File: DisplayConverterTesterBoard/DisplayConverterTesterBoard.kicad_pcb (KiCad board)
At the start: 2 copper layers, 37 x 36 mm, 25 parts, among them J2 Conn_01x07, J3 Conn_01x03, J4 FPC 20PIN P0.5mm, J5 BM20B(0.8)-10DS-0.4V, J6 Conn_01x03, J7 FPC 10PIN P0.5mm, U2 TPS61040DBV

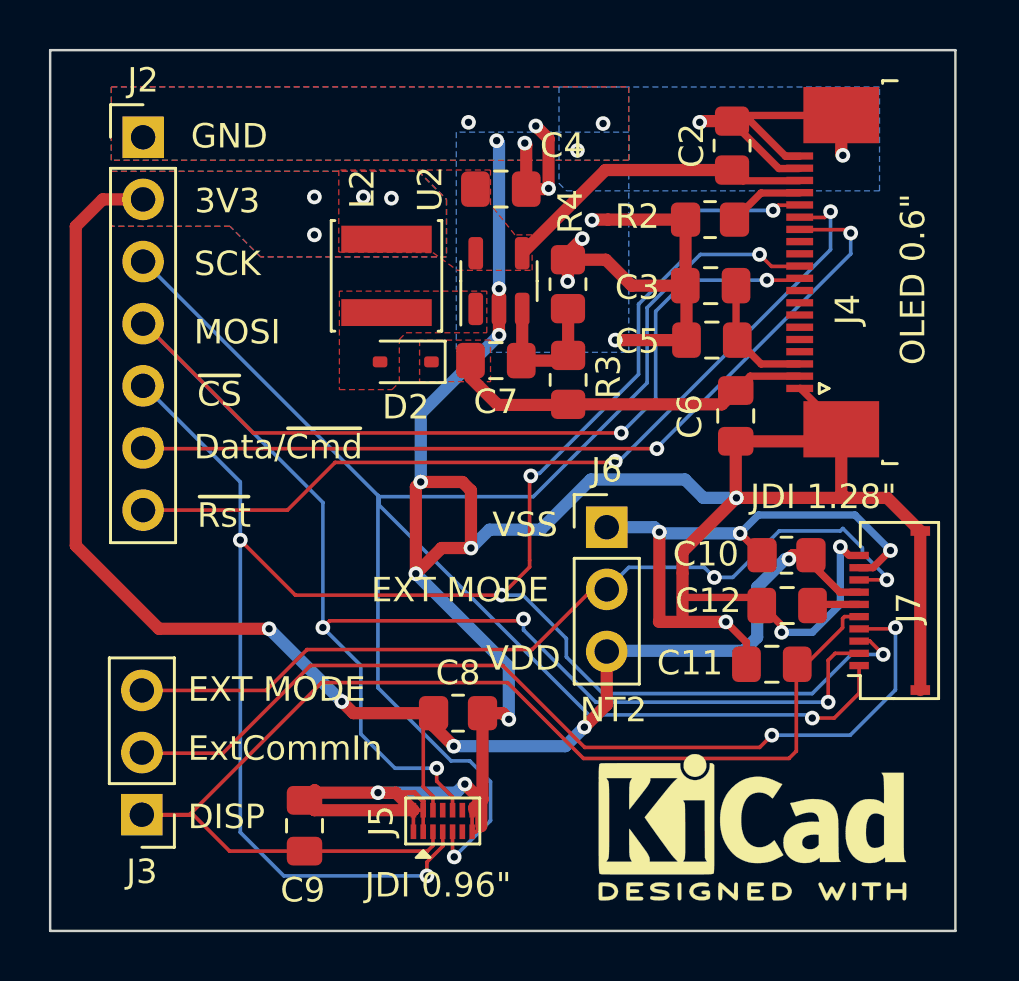
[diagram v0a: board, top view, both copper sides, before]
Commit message: updated Diode footprint. fix GND routing
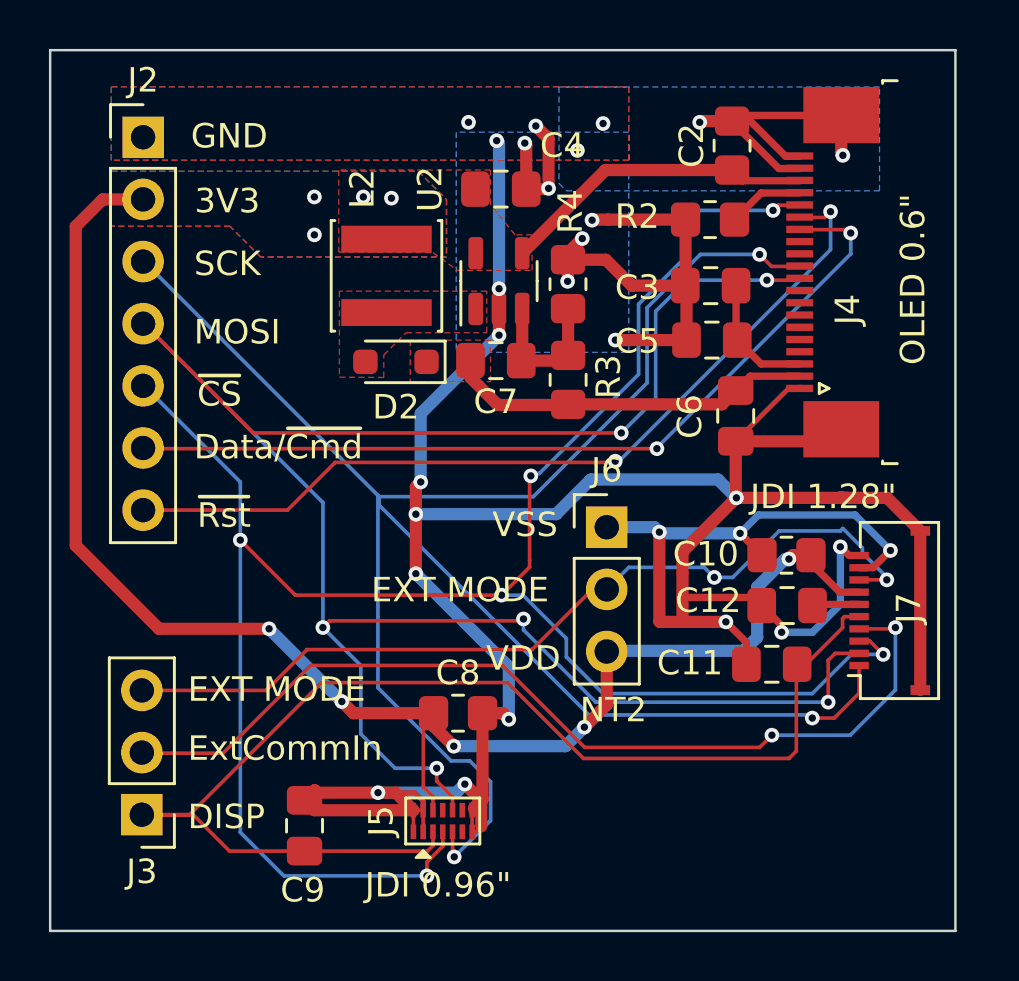
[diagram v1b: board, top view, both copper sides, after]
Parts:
- removed REF**: KiCad-Logo2_5mm_SilkScreen, Symbol:KiCad-Logo2_5mm_SilkScreen
- D2: footprint Diode_SMD:D_SOD-323 -> Diode_SMD:D_SOD-323_HandSoldering
- moved D2 0.40 mm to (100.6, 72.6)
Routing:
- net GND: track 142.5 -> 135.4 mm

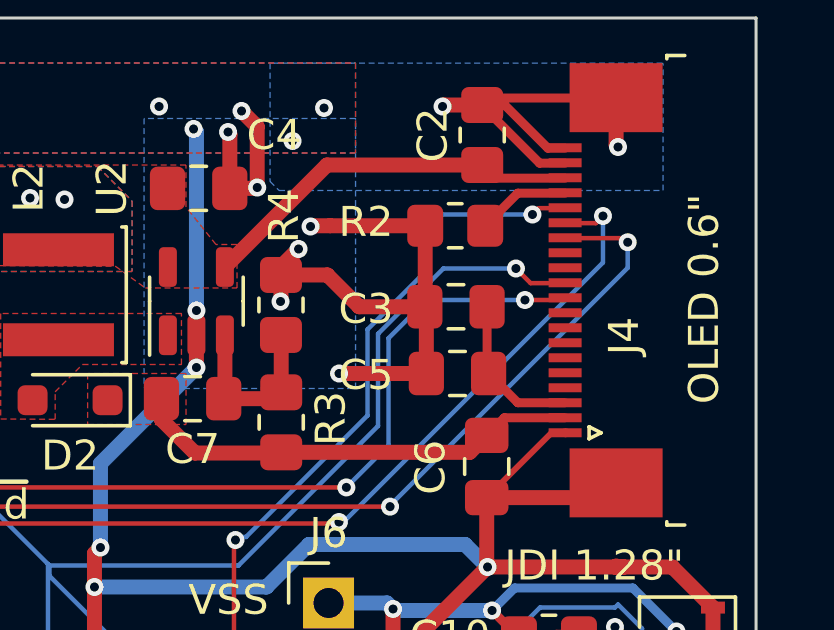
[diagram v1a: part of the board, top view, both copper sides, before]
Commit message: fix routing ( checked by HQ DFM )
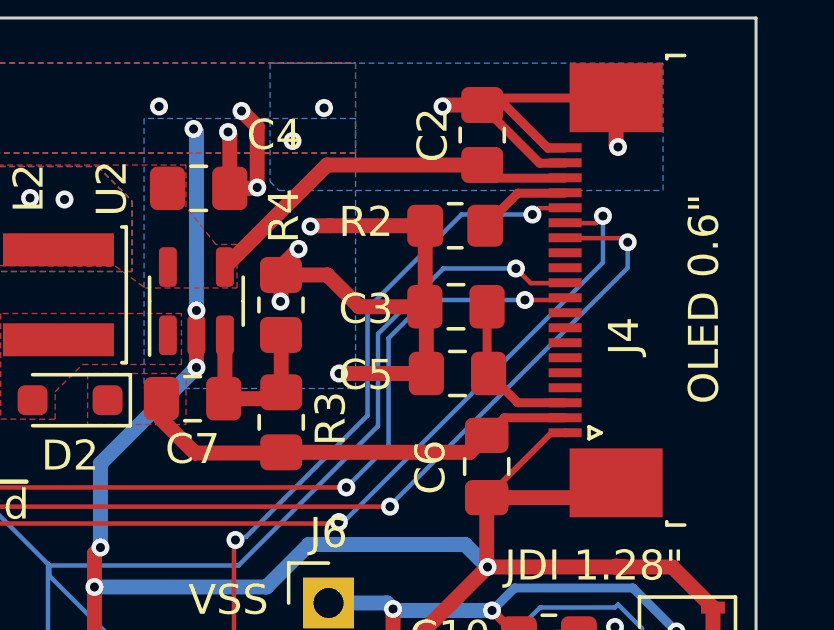
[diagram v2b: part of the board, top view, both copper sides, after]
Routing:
- net /~{CS}: track 85.4 -> 84.7 mm
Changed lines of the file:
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@@
   (via (at 106.0972 77.3006) (size 0.6) (drill 0.3) (layers "F.Cu" "B.Cu") (net 13))
   (via (at 94.2222 79.9256) (size 0.6) (drill 0.3) (layers "F.Cu" "B.Cu") (net 13))
-  (segment (start 106.0972 77.3006) (end 105.9972 77.2006) (width 0.15) (layer "B.Cu") (net 13))
-  (segment (start 106.4494 77.2006) (end 110.5 73.15) (width 0.15) (layer "B.Cu") (net 13))
+  (segment (start 110.5 73.15) (end 110.5 69.586) (width 0.15) (layer "B.Cu") (net 13))
+  (segment (start 105.9972 77.2006) (end 106.4494 77.2006) (width 0.15) (layer "B.Cu") (net 13))
   (segment (start 96 93.65) (end 94.2222 91.8722) (width 0.15) (layer "B.Cu") (net 13))
   (segment (start 119.2 84.6) (end 120.4985 84.6) (width 0.15) (layer "B.Cu") (net 13))
   (segment (start 101.85 93.65) (end 96 93.65) (width 0.15) (layer "B.Cu") (net 13))
-  (segment (start 110.5 73.15) (end 110.5 70.282852) (width 0.15) (layer "B.Cu") (net 13))
-  (segment (start 112.5472 68.235652) (end 112.5472 66.4506) (width 0.15) (layer "B.Cu") (net 13))
+  (segment (start 113.6354 66.4506) (end 115.9972 66.4506) (width 0.15) (layer "B.Cu") (net 13))
+  (segment (start 106.0972 77.3006) (end 105.9972 77.2006) (width 0.15) (layer "B.Cu") (net 13))
   (segment (start 94.2222 91.8722) (end 94.2222 79.9256) (width 0.15) (layer "B.Cu") (net 13))
   (segment (start 109.05 86.2) (end 117.6 86.2) (width 0.15) (layer "B.Cu") (net 13))
   (segment (start 94.2222 77.5506) (end 94.2222 79.9256) (width 0.15) (layer "B.Cu") (net 13))
   (segment (start 107.55 84.7) (end 109.05 86.2) (width 0.15) (layer "B.Cu") (net 13))
+  (segment (start 110.5 69.586) (end 113.6354 66.4506) (width 0.15) (layer "B.Cu") (net 13))
   (segment (start 90.3022 73.6306) (end 94.2222 77.5506) (width 0.15) (layer "B.Cu") (net 13))
   (segment (start 117.6 86.2) (end 119.2 84.6) (width 0.15) (layer "B.Cu") (net 13))
@@
   (segment (start 107.55 83.95) (end 107.55 84.7) (width 0.15) (layer "B.Cu") (net 13))
   (segment (start 104.9 82.1756) (end 105.7756 82.1756) (width 0.15) (layer "B.Cu") (net 13))
-  (segment (start 105.9972 77.2006) (end 106.4494 77.2006) (width 0.15) (layer "B.Cu") (net 13))
-  (segment (start 112.5472 66.4506) (end 115.9972 66.4506) (width 0.15) (layer "B.Cu") (net 13))
   (segment (start 90.2972 73.6306) (end 90.3022 73.6306) (width 0.15) (layer "B.Cu") (net 13))
-  (segment (start 110.5 70.282852) (end 112.5472 68.235652) (width 0.15) (layer "B.Cu") (net 13))
+  (segment (start 106.4494 77.2006) (end 110.5 73.15) (width 0.15) (layer "B.Cu") (net 13))
   (segment (start 111.25 76.1881) (end 90.2747 76.1881) (width 0.15) (layer "F.Cu") (net 14))
   (segment (start 119.0354 67.2388) (end 117.0858 67.2388) (width 0.15) (layer "F.Cu") (net 14))

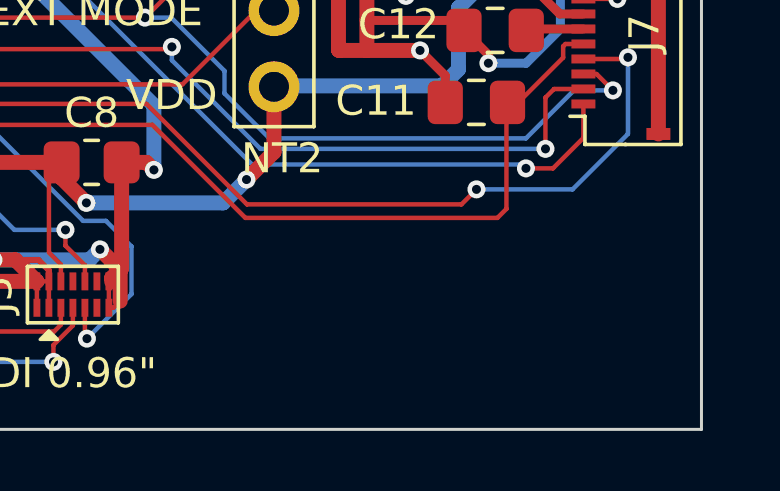
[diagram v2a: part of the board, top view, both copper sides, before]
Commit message: added Kicad logo
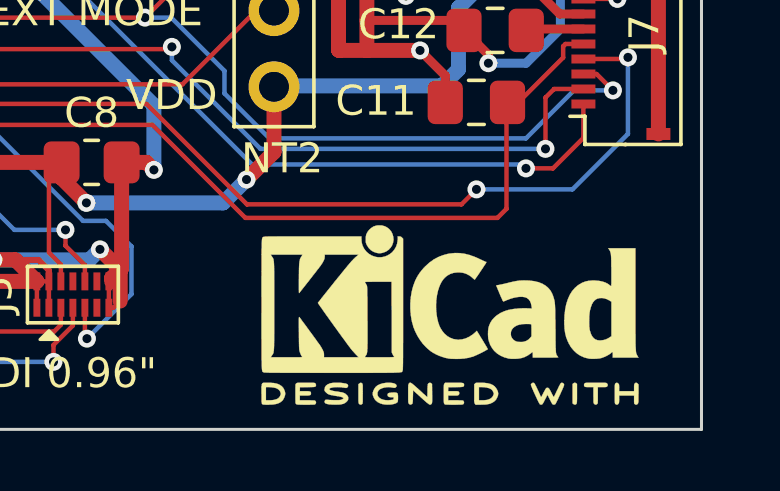
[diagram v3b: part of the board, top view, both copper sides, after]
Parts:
- added REF**: KiCad-Logo2_5mm_SilkScreen, Symbol:KiCad-Logo2_5mm_SilkScreen, F.Cu at (115.1, 92.1)
